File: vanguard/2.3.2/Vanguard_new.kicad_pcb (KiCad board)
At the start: 4 copper layers, 46.4 x 51.9 mm, 93 parts, among them J1 USB_C_Receptacle_USB2.0_16P, J2 Conn_02x03_Pin, J3 Micro_SD_Card_Det1, J4 STARBOARD_SERVO, J5 PORTSIDE_SERVO, J6 Battery In, J7 EJECTION_SERVO, Q1 BSS138, Q2 BSS138, Q3 BSS138, Q4 BSS138, U1 ATSAMD11D14A-M, U10 BMP390L, U2 ATmega4809-A, U3 AT25DF641A-SH-T, U4 AP2112K-3.3, U5 BD1020HFV, U6 BNO086, U7 TXB0104D, U8 TPS61092, U9 MPM3610AGQV-P, Y1 32.768kHz

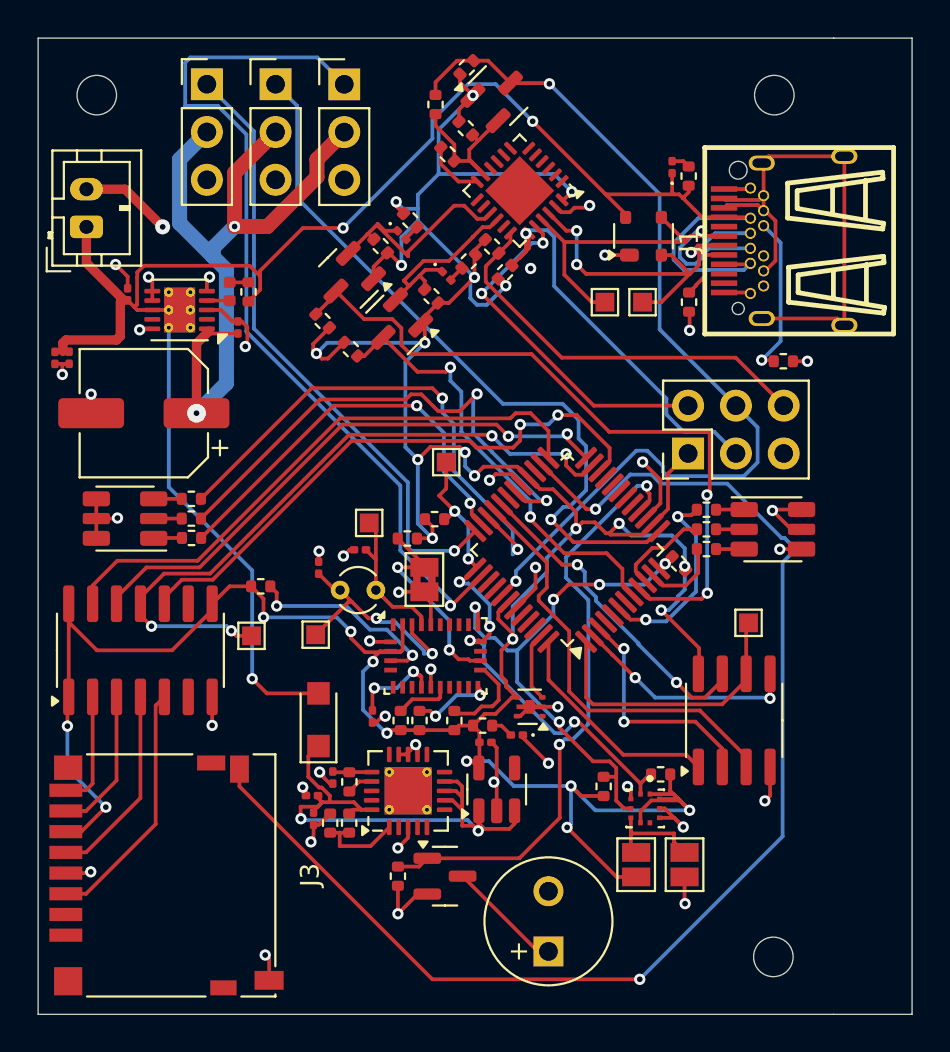
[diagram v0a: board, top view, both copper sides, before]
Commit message: 2.3.2 created, 2.4.1 removed
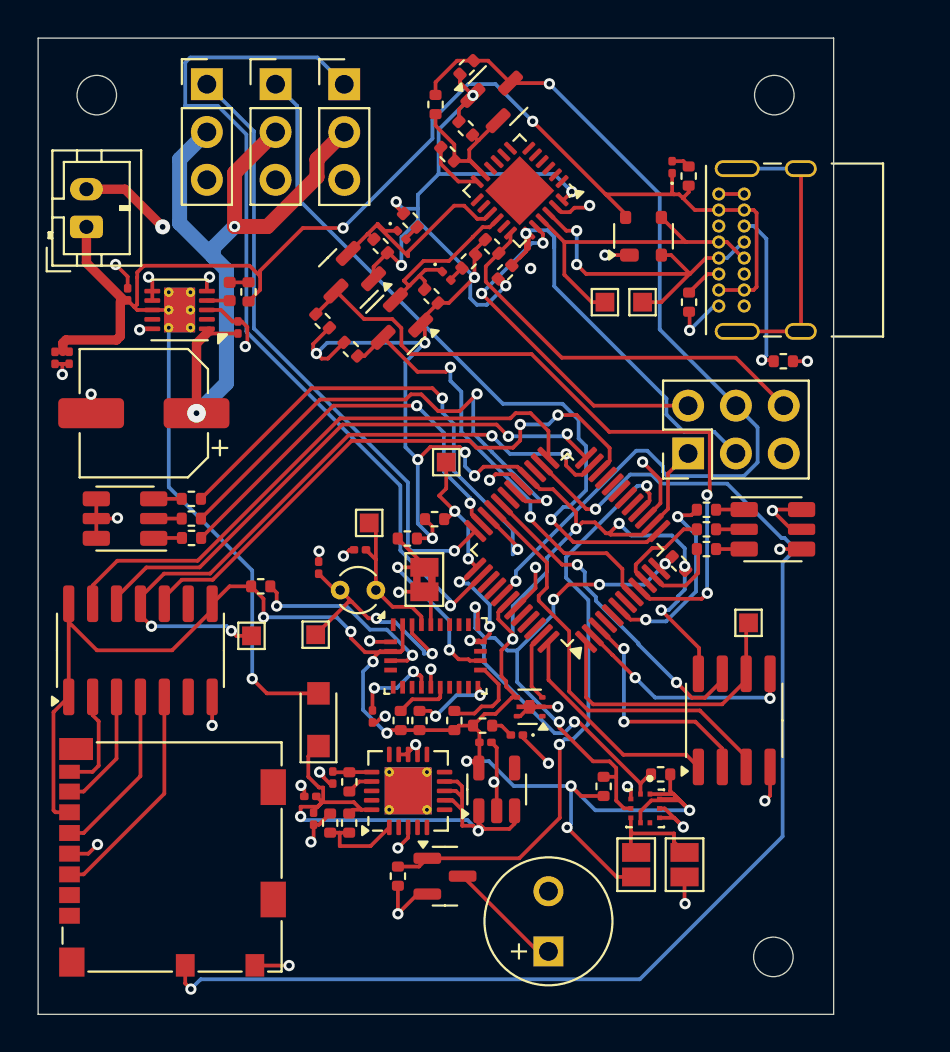
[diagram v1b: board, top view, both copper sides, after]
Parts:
- J1: footprint Connector_USB:USB-C-SMD_JLC REPLACEMENT -> Connector_USB:USB_C_Receptacle_GCT_USB4085
- J3: footprint Connector_Card:microSD_HC_Hirose_DM3D-SF -> Connector_Card:microSD_HC_Molex_104031-0811
- moved J1 4.91 mm to (128.6, 98.2)
- moved J3 1.00 mm to (99.5, 127.5), turned to 90 degrees
- moved C5 0.10 mm to (106.8, 124.3)
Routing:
- net (no net): track 29.0 -> 0.00 mm
- net unconnected-(J1-SHIELD-PadS1): track 0.00 -> 15.4 mm
- net Net-(D1-I/O2): track 24.3 -> 17.9 mm, vias 1 -> 0
- net BATT_IN: track 97.9 -> 92.7 mm
- net Net-(D1-I/O1): track 23.2 -> 18.5 mm, vias 3 -> 2
- net +3.3V: track 201.1 -> 198.9 mm, vias 27 -> 25
- net GND: track 76.5 -> 77.9 mm
- net Net-(J1-CC1): track 3.33 -> 2.00 mm
- net Net-(J3-DAT0): track 7.81 -> 6.50 mm
- net Net-(J3-CLK): track 10.5 -> 9.23 mm
- net Net-(J3-CMD): track 13.3 -> 12.0 mm
- net CD: track 69.4 -> 68.4 mm
- net Net-(J3-DAT1): track 6.18 -> 5.47 mm
- net Net-(J2-Pin_3): track 21.7 -> 22.3 mm
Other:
- board size 46.4 x 51.9 mm -> 42.3 x 51.9 mm
